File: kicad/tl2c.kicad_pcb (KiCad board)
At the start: 4 copper layers, 119.4 x 127 mm, 87 parts, among them IC101 ATTINY20-X, P101 12VDC, P102 I2C Master, P103 Spare, P104 ISP Header, P105 LED_DRIVER, P106 240VAC, P107 LED_DRIVER, P108 LED_OUT, P301 PIR13, Q301 IRLML2502, Q302 IRLML2502, Q303 IRLML2502, Q401 IRLML2502, Q402 IRLML2502, Q403 IRLML2502, SW101 TL3315NF160Q, U201 LF120ABDT-TR, U202 TPS70933

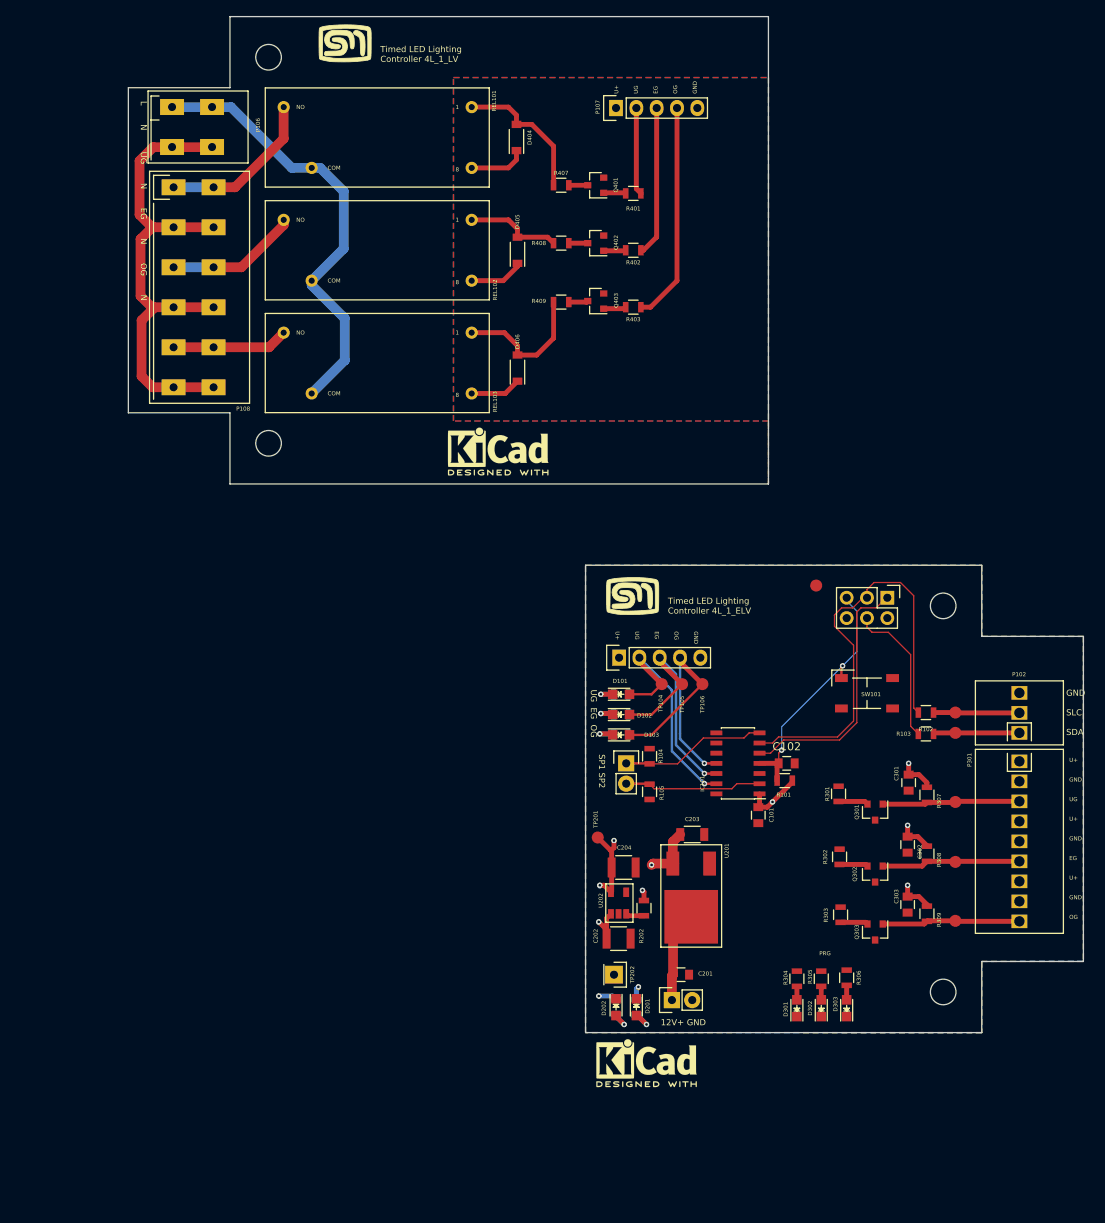
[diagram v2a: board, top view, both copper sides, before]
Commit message: Finished off the refactoring for the housing and terminal blocks
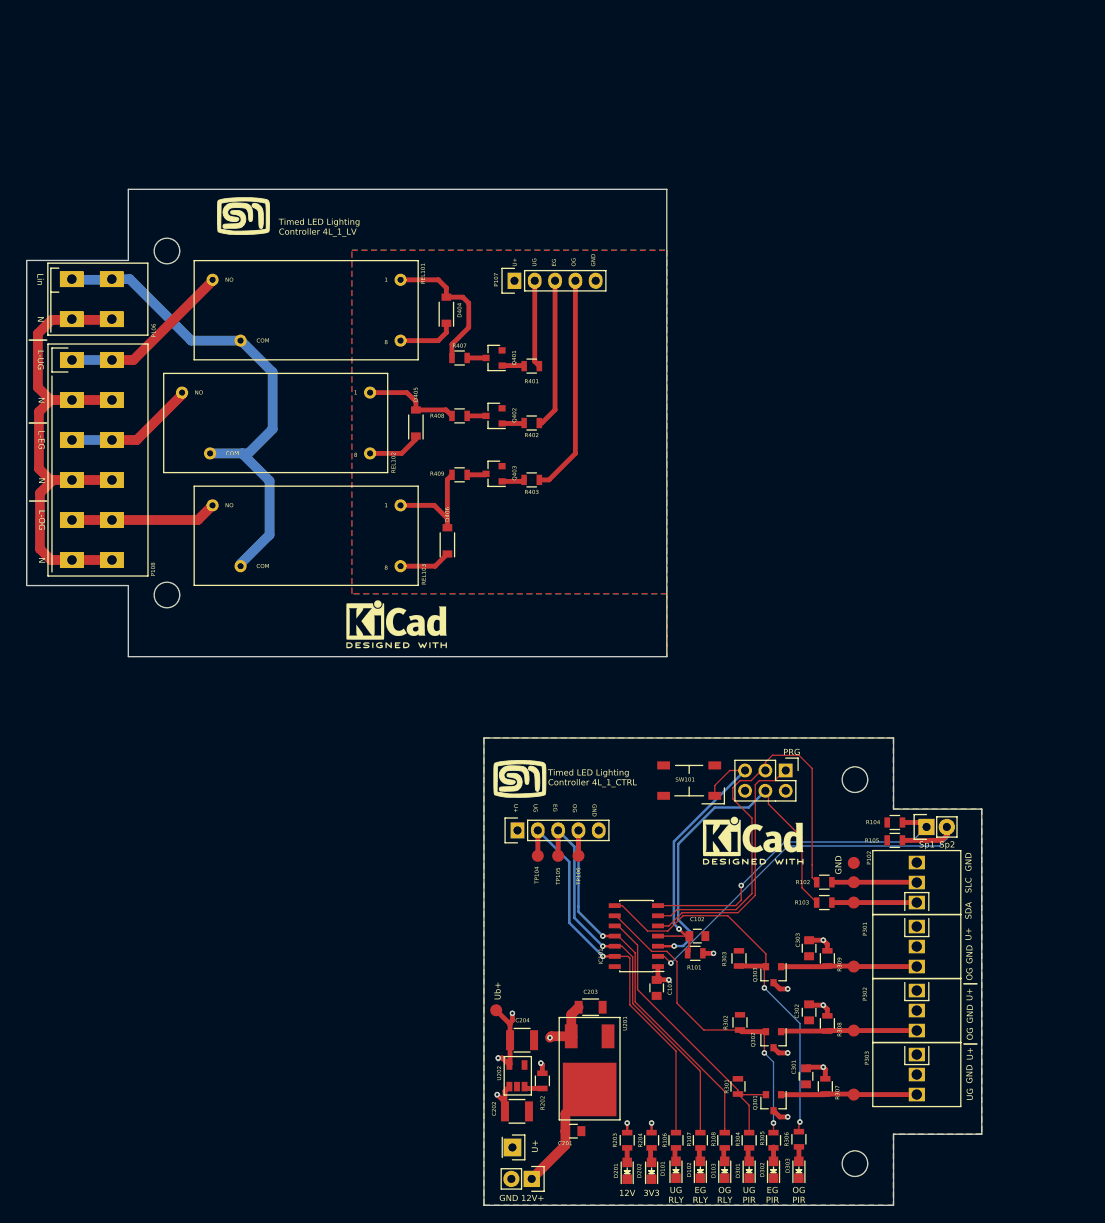
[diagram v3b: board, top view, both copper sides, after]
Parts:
- added P302: CONN_PIR_EG, tl2c-footprint:Spring_Terminal_Block_1_x_3, F.Cu at (146.8, 152.2)
- added P303: CONN_PIR_UG, tl2c-footprint:Spring_Terminal_Block_1_x_3, F.Cu at (146.8, 160.2)
- P301: value PIR13 -> CONN_PIR_OG; footprint tl2c-footprint:Spring_Terminal_Block_1_x_9 -> tl2c-footprint:Spring_Terminal_Block_1_x_3
- R106, R107, R108, R203, R204: moved to F.Cu
- moved D101 59.8 mm to (116.7, 174.6), turned to 90 degrees
- moved D102 57.8 mm to (119.8, 174.6), turned to 90 degrees
- moved R106 56.2 mm to (116.7, 170.9), turned to 270 degrees
- moved D103 55.9 mm to (122.8, 174.6), turned to 90 degrees
- moved R107 54.1 mm to (119.8, 170.9), turned to 270 degrees
- moved R108 52.3 mm to (122.8, 170.9), turned to 270 degrees
- moved C301 38.9 mm to (133.0, 162.9)
- moved TP301 38.7 mm to (138.9, 165.2)
- moved R301 38.7 mm to (124.5, 164.2)
- moved R307 38.6 mm to (135.4, 164.2)
- moved Q301 38.5 mm to (128.9, 166.2)
- moved P103 38.4 mm to (148.0, 131.8), turned to 90 degrees
- moved TP101 35.0 mm to (138.9, 136.3)
- moved R104 31.8 mm to (144.1, 131.2), turned to 0 degrees
- moved R105 31.3 mm to (144.1, 133.5), turned to 0 degrees
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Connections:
- D101 pad 1: Net-(D101-Pad1) -> GND
- D101 pad 2: /RelayUG -> Net-(D101-Pad2)
- D102 pad 1: Net-(D102-Pad1) -> GND
- D102 pad 2: /RelayEG -> Net-(D102-Pad2)
- D103 pad 1: Net-(D103-Pad1) -> GND
- D103 pad 2: /RelayOG -> Net-(D103-Pad2)
- P301 pad 3: /PIR13/PIR_UG -> /PIR13/PIR_OG
- R106 pad 1: Net-(D101-Pad1) -> /RelayUG
- R106 pad 2: GND -> Net-(D101-Pad2)
- R107 pad 1: Net-(D102-Pad1) -> /RelayEG
- R107 pad 2: GND -> Net-(D102-Pad2)
- R108 pad 1: Net-(D103-Pad1) -> /RelayOG
- R108 pad 2: GND -> Net-(D103-Pad2)
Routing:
- net /PIR13/SIG_OG: track 3.45 -> 50.6 mm, vias 0 -> 2
- net /PIR13/SIG_EG: track 3.58 -> 41.1 mm, vias 0 -> 2
- net /Spare2: track 17.2 -> 52.6 mm, vias 0 -> 1
- net /PIR13/SIG_UG: track 4.43 -> 37.3 mm
- net /MOSI: track 18.3 -> 47.7 mm, vias 0 -> 1
- net /Spare1: track 18.6 -> 42.2 mm, vias 0 -> 1
- net /RelayUG: track 29.6 -> 50.5 mm
- net /RelayEG: track 30.9 -> 50.2 mm
- net /RelayOG: track 32.2 -> 50.2 mm
- net /Lin: track 56.0 -> 63.1 mm
- net /~Reset: track 31.6 -> 37.4 mm, vias 2 -> 1
- net /Power System/U+In: track 11.6 -> 17.4 mm
- net /LineOG: track 14.5 -> 18.3 mm
- net /PIR13/U+: track 29.7 -> 26.1 mm
- net Net-(D103-Pad1): track 3.44 -> 0.00 mm, vias 1 -> 0
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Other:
- outline, holes or cut-outs redrawn
- board text added: "12V"
- board text added: "3V3"
- board text added: "EG PIR"
- board text added: "EG RLY"
- board text added: "GND"
- board text added: "GND 12V+"
- board text added: "L-EG"
- board text added: "L-OG"
- board text added: "L-UG"
- board text added: "Lin"
- board text added: "N"
- board text added: "OG"
- board text added: "OG PIR"
- board text added: "OG RLY"
- board text added: "SDA"
- board text added: "SLC"
- board text added: "Sp1"
- board text added: "Sp2"
- board text added: "Timed LED Lighting Controller 4L_1_CTRL"
- board text added: "U+"
- board text added: "UG"
- board text added: "UG PIR"
- board text added: "UG RLY"
- board text added: "Ub+"
- board text removed: "12V+ GND"
- board text removed: "GND SLC SDA"
- board text removed: "L N UG N EG N OG N"
- board text removed: "SP1 SP2"
- board text removed: "Timed LED Lighting Controller 4L_1_ELV"
- board text removed: "U+ GND UG U+ GND EG U+ GND OG"
- board text removed: "UG EG OG"

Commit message: Included a small fuse on the Active. Finalised the board
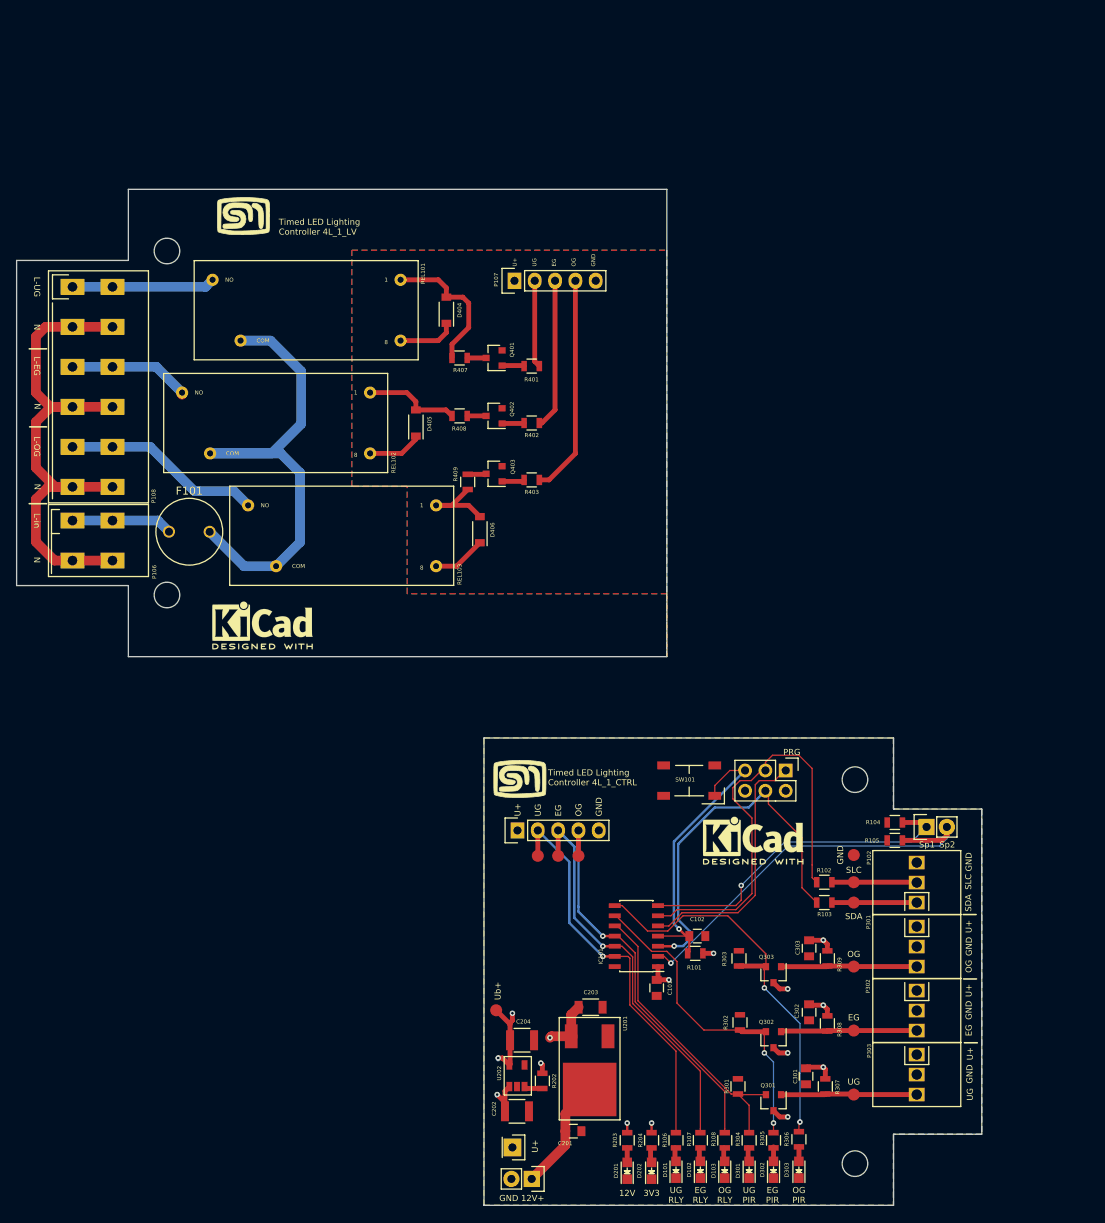
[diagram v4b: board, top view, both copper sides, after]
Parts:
- added F101: 500mA, tl2c-footprint:Fuse_TE5_Littlefuse-ESKA_887_O14, F.Cu at (55.9, 94.9)
- moved P106 30.2 mm to (41.3, 93.5)
- moved REF*** 16.8 mm to (65.0, 106.6)
- moved P108 9.14 mm to (41.3, 64.3)
- moved REL103 4.45 mm to (74.9, 95.4)
- moved D406 4.30 mm to (92.2, 94.6)
- moved R409 1.35 mm to (90.7, 88.6), turned to 90 degrees
- moved TP101 0.99 mm to (138.9, 135.3)
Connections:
- P107 pad 1: /LED Driver/LED_DRIVER_U+ -> Net-(P107-Pad1)
- P107 pad 2: /LED Driver/Relay_UG -> Net-(P107-Pad2)
- P107 pad 3: /LED Driver/Relay_EG -> Net-(P107-Pad3)
- P107 pad 4: /LED Driver/Relay_OG -> Net-(P107-Pad4)
- REL101 pad 6: /Lin -> Net-(F101-Pad2)
- REL102 pad 6: /Lin -> Net-(F101-Pad2)
- REL103 pad 6: /Lin -> Net-(F101-Pad2)
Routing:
- net Net-(F101-Pad2): track 0.00 -> 64.0 mm
- net /Lin: track 63.1 -> 12.6 mm
- net Net-(P107-Pad4): track 0.00 -> 21.6 mm
- net /LED Driver/Relay_OG: track 27.5 -> 5.88 mm
- net Net-(P107-Pad3): track 0.00 -> 16.1 mm
- net /LED Driver/Relay_EG: track 18.8 -> 2.65 mm
- net Net-(P107-Pad2): track 0.00 -> 10.1 mm
- net /LED Driver/Relay_UG: track 10.9 -> 0.80 mm
- net /LineOG: track 18.3 -> 25.0 mm
- net /Neutral: track 64.5 -> 70.1 mm, vias 1 -> 0
- net /LineUG: track 21.8 -> 17.9 mm
- net Net-(D406-Pad2): track 14.4 -> 10.8 mm
- net /LineEG: track 16.4 -> 15.3 mm
- net /PIR13/SIG_UG: track 37.3 -> 38.1 mm
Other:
- board size 119.4 x 127 mm -> 120.7 x 127 mm
- board text added: "EG"
- board text added: "L-in"
- board text removed: "GND OG EG UG U+"
- board text removed: "Lin"

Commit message: Finilised the layout with a larger pin header to expose spare pins to relay driver board
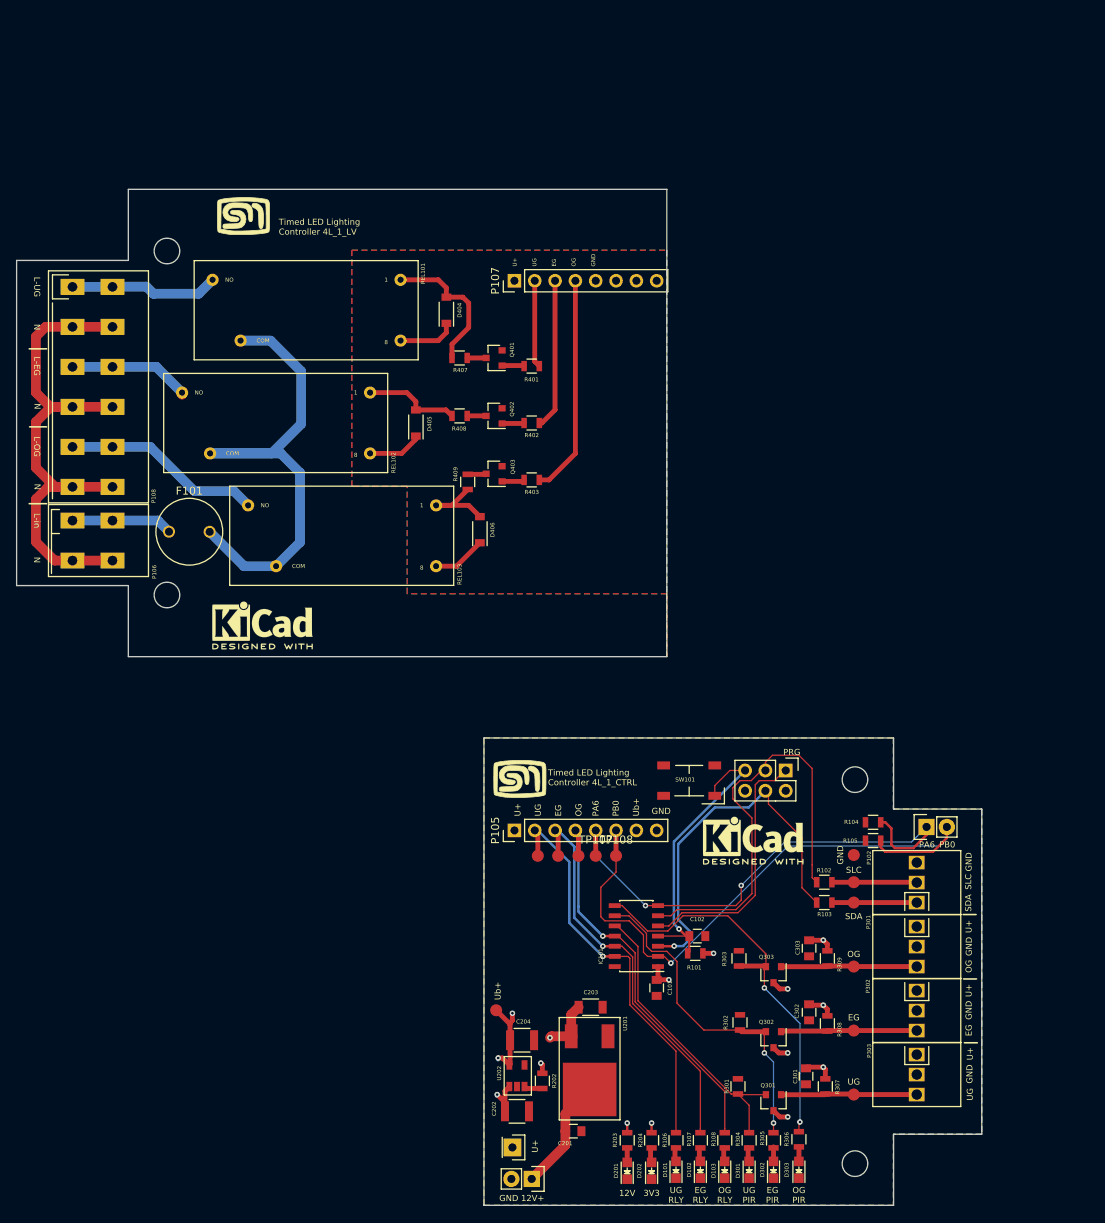
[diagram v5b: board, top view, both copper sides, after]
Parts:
- added TP107: PA6, Measurement_Points:Measurement_Point_Round-SMD-Pad_Small, F.Cu at (106.7, 135.4)
- added TP108: PB0, Measurement_Points:Measurement_Point_Round-SMD-Pad_Small, F.Cu at (109.2, 135.4)
- P105, P107: footprint Pin_Headers:Pin_Header_Straight_1x05 -> Pin_Headers:Pin_Header_Straight_1x08_Pitch2.54mm
- moved R104 2.72 mm to (141.4, 131.2)
- moved R105 2.72 mm to (141.4, 133.5)
- moved P105 0.38 mm to (96.5, 132.2)
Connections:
- IC101 pad 2: /Spare2 -> /GPIO_PB0
- IC101 pad 7: /Spare1 -> /GPIO_PA6
- P103 pad 1: /Spare1 -> /GPIO_PA6
- P103 pad 2: /Spare2 -> /GPIO_PB0
- P105 pad 5: GND -> /GPIO_PA6
- P107 pad 1: Net-(P107-Pad1) -> /LED Driver/LED_DRIVER_U+
- P107 pad 2: Net-(P107-Pad2) -> /LED Driver/Relay_UG
- P107 pad 3: Net-(P107-Pad3) -> /LED Driver/Relay_EG
- P107 pad 4: Net-(P107-Pad4) -> /LED Driver/Relay_OG
- P107 pad 5: GNDA -> Net-(P107-Pad5)
- R104 pad 2: /Spare1 -> /GPIO_PA6
- R105 pad 2: /Spare2 -> /GPIO_PB0
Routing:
- net /GPIO_PB0: track 0.00 -> 79.2 mm, vias 0 -> 1
- net /GPIO_PA6: track 0.00 -> 66.4 mm, vias 0 -> 2
- net /Spare2: track 52.6 -> 0.00 mm, vias 1 -> 0
- net /Spare1: track 42.2 -> 0.00 mm, vias 1 -> 0
- net Net-(P107-Pad4): track 21.6 -> 0.00 mm
- net /LED Driver/Relay_OG: track 5.88 -> 27.5 mm
- net Net-(P107-Pad3): track 16.1 -> 0.00 mm
- net /LED Driver/Relay_EG: track 2.65 -> 18.8 mm
- net Net-(P107-Pad2): track 10.1 -> 0.00 mm
- net /LED Driver/Relay_UG: track 0.80 -> 10.9 mm
- net /PIR13/SIG_EG: track 41.1 -> 42.2 mm
- net /LineUG: track 17.9 -> 18.6 mm
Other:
- board text added: "PA6"
- board text added: "PB0"
- board text removed: "Sp1"
- board text removed: "Sp2"
